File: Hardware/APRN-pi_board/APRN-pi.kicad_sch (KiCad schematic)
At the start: 21 parts, among them J1 Raspberry_Pi_2_3, J2 Conn_Coaxial, J3 Amplifier Jumper, Q1 2N3906, U1 DRA818V

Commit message: Flip header correct direction
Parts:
- J1: footprint Connector_PinHeader_2.54mm:PinHeader_2x20_P2.54mm_Vertical -> Connector_PinSocket_2.54mm:PinSocket_2x20_P2.54mm_Vertical
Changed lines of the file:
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@@
       (effects (font (size 1.27 1.27)) (justify left))
     )
-    (property "Footprint" "Connector_PinHeader_2.54mm:PinHeader_2x20_P2.54mm_Vertical" (id 2) (at 140.97 100.33 0)
+    (property "Footprint" "Connector_PinSocket_2.54mm:PinSocket_2x20_P2.54mm_Vertical" (id 2) (at 140.97 100.33 0)
       (effects (font (size 1.27 1.27)) hide)
     )
@@
     )
     (path "/3f3bf25c-fe77-4cf4-b69b-53b67dff8a67"
-      (reference "J1") (unit 1) (value "Raspberry_Pi_2_3") (footprint "Connector_PinHeader_2.54mm:PinHeader_2x20_P2.54mm_Vertical")
+      (reference "J1") (unit 1) (value "Raspberry_Pi_2_3") (footprint "Connector_PinSocket_2.54mm:PinSocket_2x20_P2.54mm_Vertical")
     )
     (path "/5791b404-6cc9-43a8-ab1e-d5acafca7fe6"

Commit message: Hook up voltage regulator
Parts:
- added C4: 10u, Capacitor_SMD:C_0805_2012Metric, symbol Device:C_Small
- added C5: 0.1u, Capacitor_SMD:C_0805_2012Metric, symbol Device:C_Small
- added J4: Screw_Terminal_01x02, TerminalBlock:TerminalBlock_bornier-2_P5.08mm, symbol Connector:Screw_Terminal_01x02
- added U2: L7805, Package_TO_SOT_THT:TO-220-3_Vertical, symbol Regulator_Linear:L7805
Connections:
- net +5V: now also C5.1, U2.3 (OUT)
- net GND: now also C4.2, C5.2, J4.1 (Pin_1), U2.2 (GND)
- new net: C4.1, J4.2 (Pin_2), U2.1 (IN)

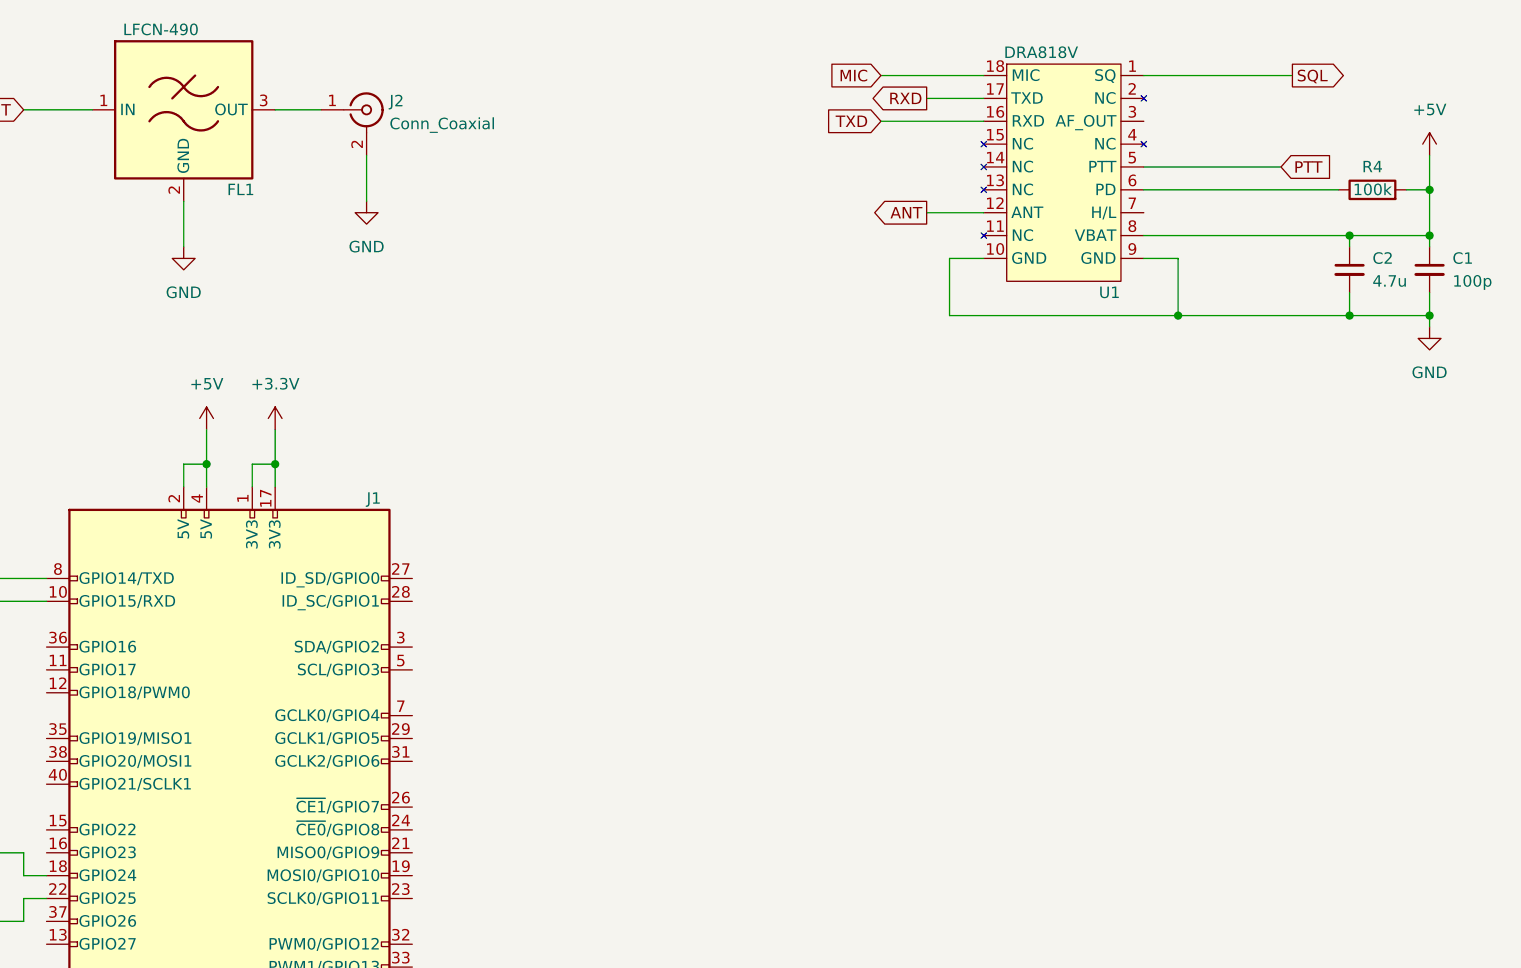
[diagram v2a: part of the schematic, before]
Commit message: More power and audio cleanup
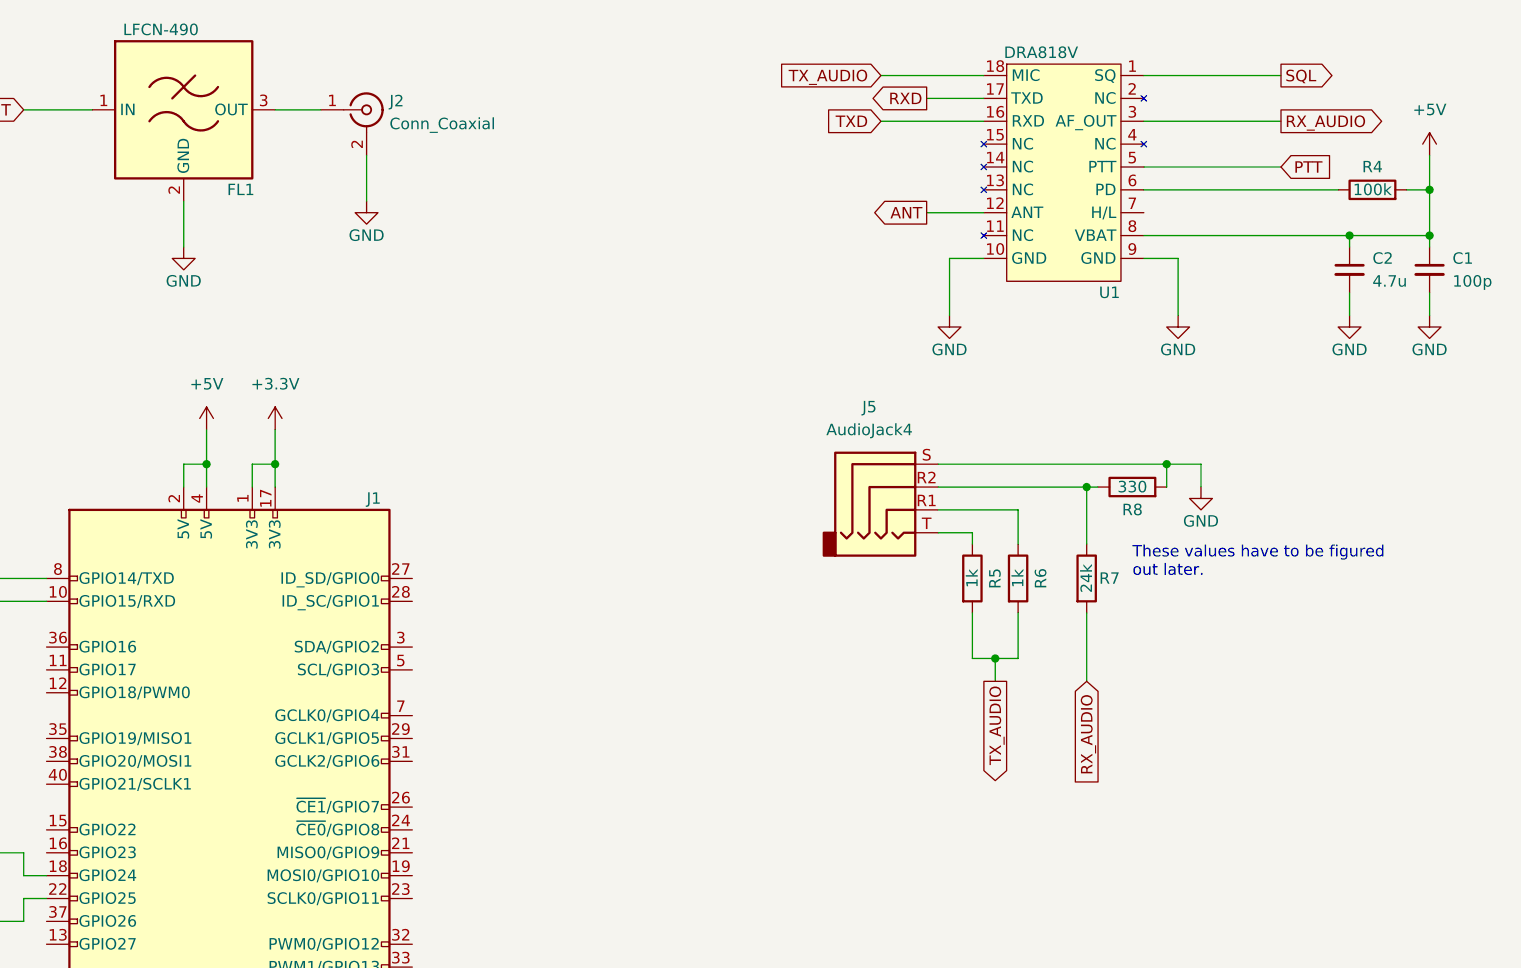
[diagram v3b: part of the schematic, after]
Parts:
- added J5: AudioJack4, Connector_Audio:Jack_3.5mm_PJ320E_Horizontal, symbol Connector:AudioJack4
- added R5, R6: 1k, Resistor_SMD:R_0805_2012Metric, symbol Device:R
- added R7: 24k, Resistor_SMD:R_0805_2012Metric, symbol Device:R
- added R8: 330, Resistor_SMD:R_0805_2012Metric, symbol Device:R
- H1, H2, H3, H4: footprint MountingHole:MountingHole_2.2mm_M2 -> MountingHole:MountingHole_2.7mm
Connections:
- net GND: now also J5.S, R8.2
- net RX_AUDIO: now reaches U1.3 (AF_OUT)
- net RX_AUDIO: now also R7.2
- net MIC renamed TX_AUDIO
- net TX_AUDIO: now also R5.2, R6.2
- new net: J5.R2, R7.1, R8.1
- new net: J5.R1, R6.1
- new net: J5.T, R5.1
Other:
- note added: "These values have to be figured out later."

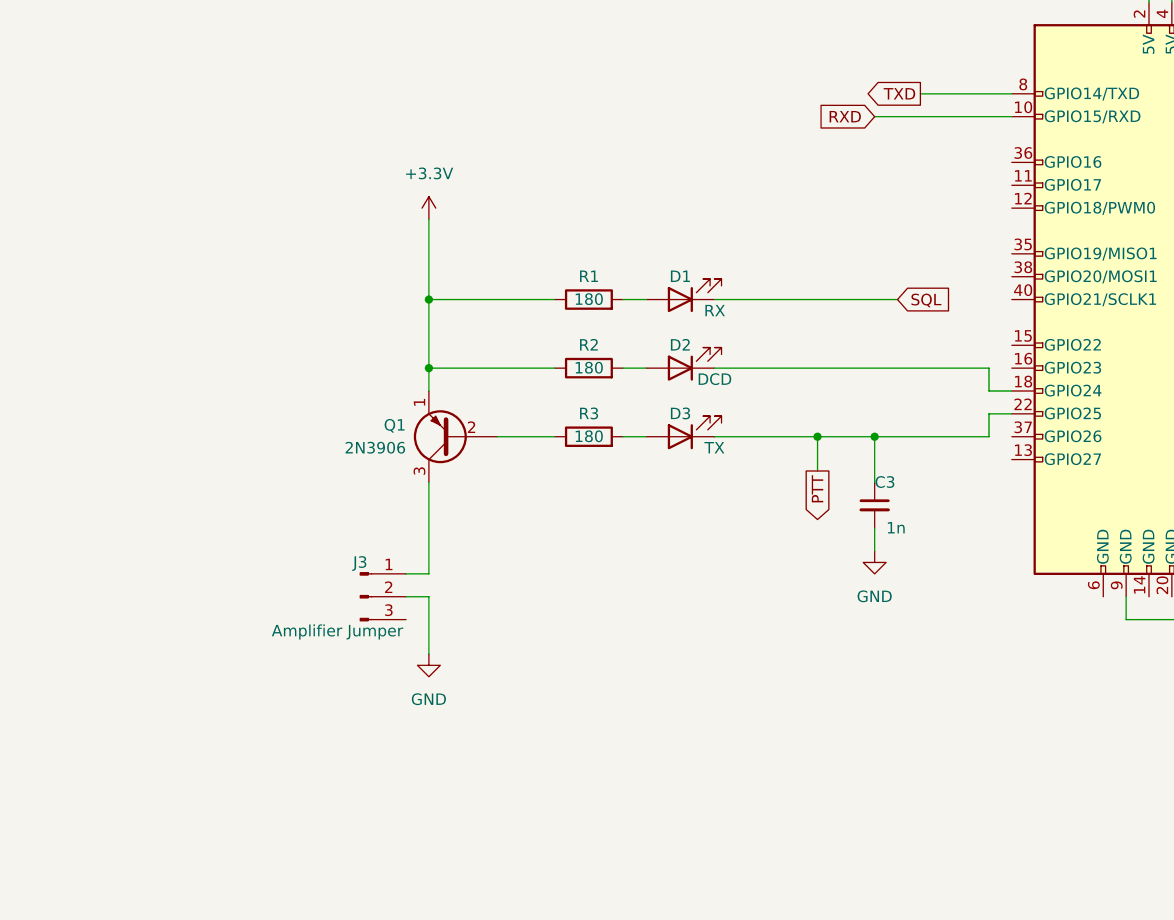
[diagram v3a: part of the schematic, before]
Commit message: GPIO22 should read input rx as input
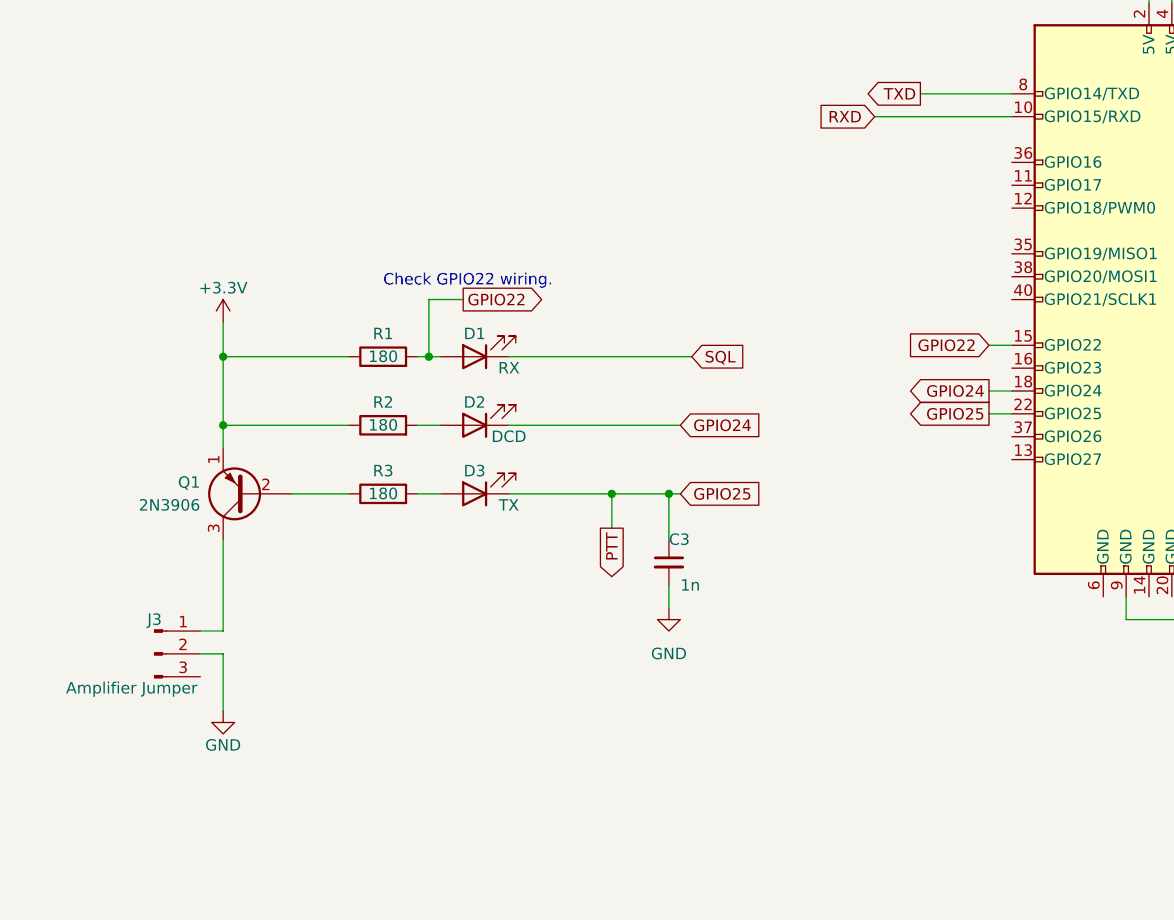
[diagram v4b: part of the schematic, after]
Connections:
- net GPIO24: now reaches D2.1 (K), J1.18 (GPIO24)
- net GPIO22: now reaches J1.15 (GPIO22)
- net GPIO22: now also D1.2 (A), R1.2
- net PTT renamed GPIO25
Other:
- note added: "Check GPIO22 wiring."
- moved on the sheet: C3, D1, D2, D3, J3, Q1, R1, R2, R3

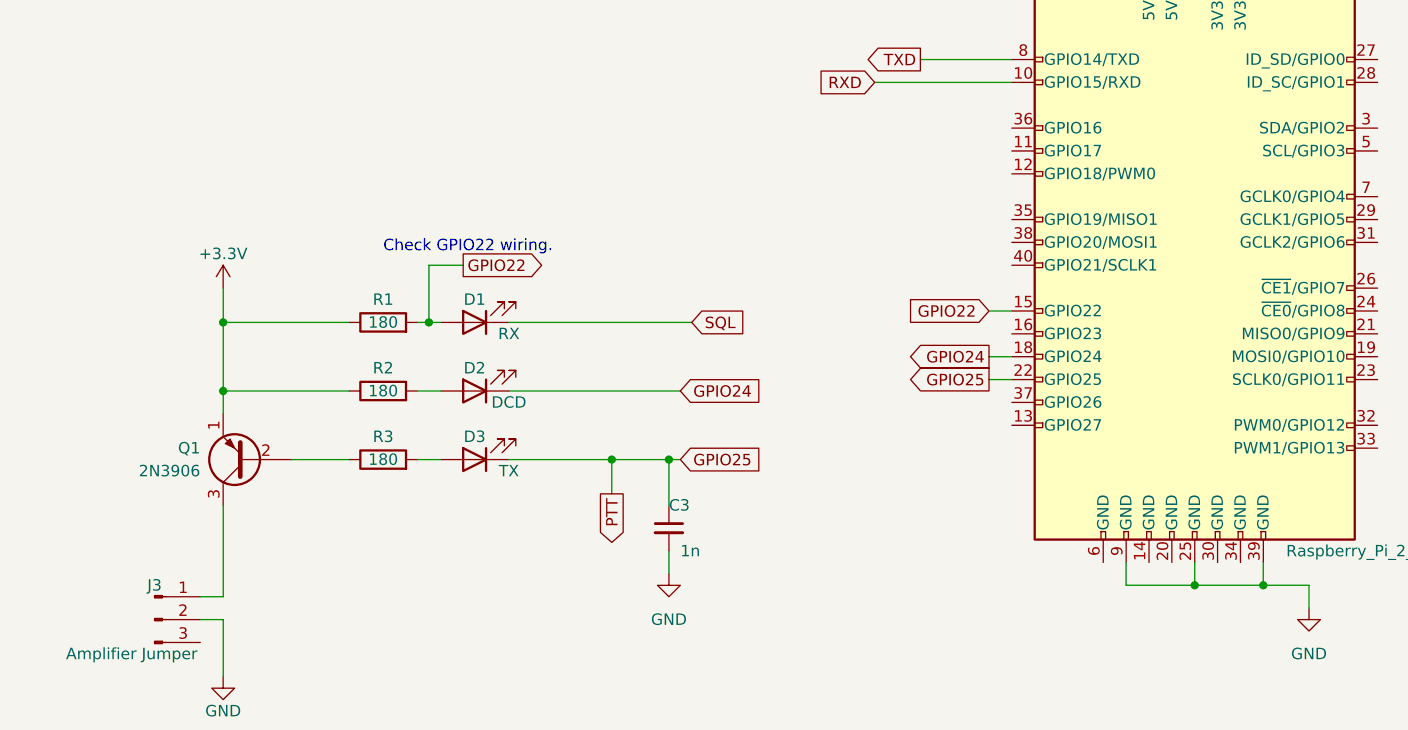
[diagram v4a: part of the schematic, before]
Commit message: Clean schematic a little
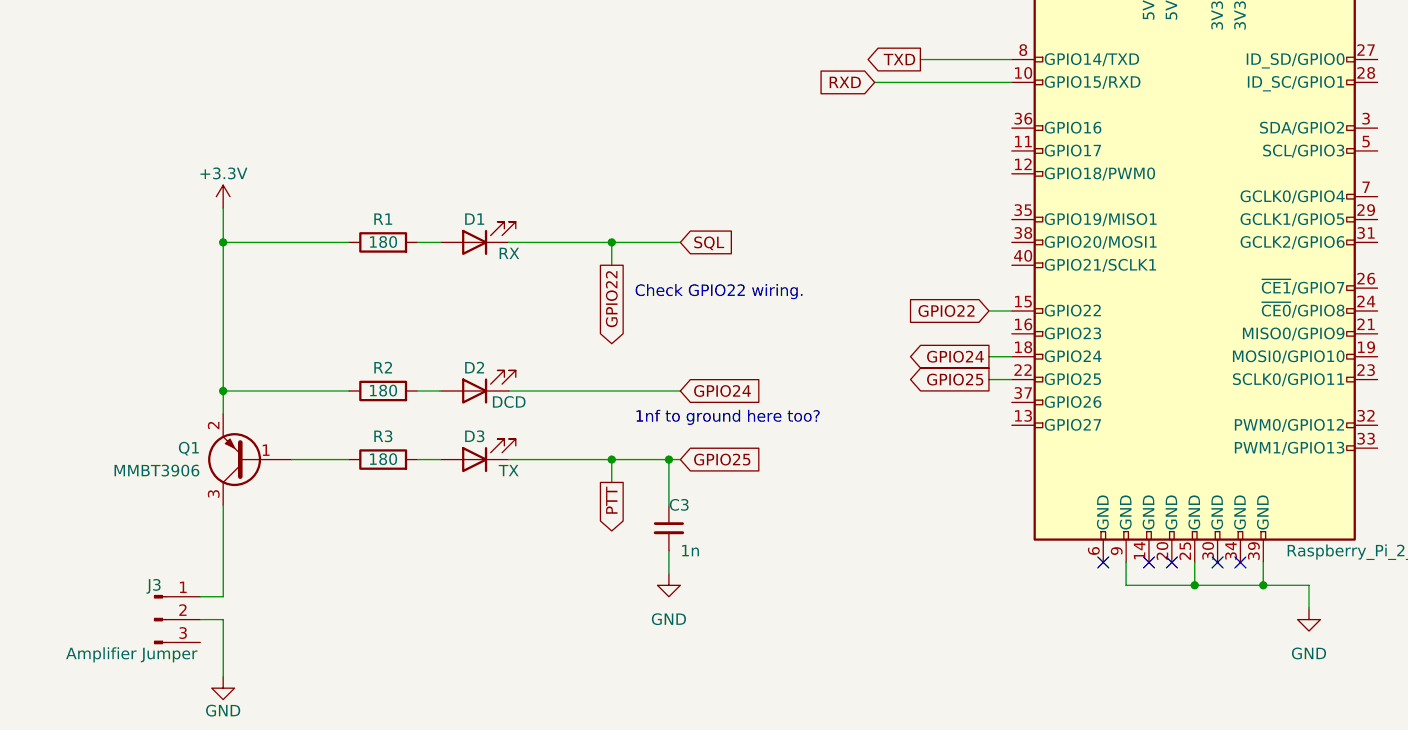
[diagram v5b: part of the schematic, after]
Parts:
- removed Q1: 2N3906, Package_TO_SOT_THT:TO-92_Inline, symbol Transistor_BJT:2N3906
- added Q1: MMBT3906, Package_TO_SOT_SMD:SOT-23, symbol Transistor_BJT:MMBT3906
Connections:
- net SQL is gone; now on net GPIO22: D1.1 (K), U1.1 (SQ)
- net +3V3: now also Q1.2 (E)
- net GPIO22: no longer D1.2 (A), R1.2
- net at J3.1 (Pin_1): now also Q1.3 (C)
- net at R3.1: now also Q1.1 (B)
- new net: D1.2 (A), R1.2
- no-connect marks 0 -> 5
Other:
- note added: "1nf to ground here too?"
- moved on the sheet: D1, R1
